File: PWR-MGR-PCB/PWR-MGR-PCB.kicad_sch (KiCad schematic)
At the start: 19 parts, among them J1 USB_C_Receptacle_USB2.0_14P, J2 Battery_1x2, U1 USBLC6-2SC6, U2 TLV75533PDBV, U3 BQ24074RGT

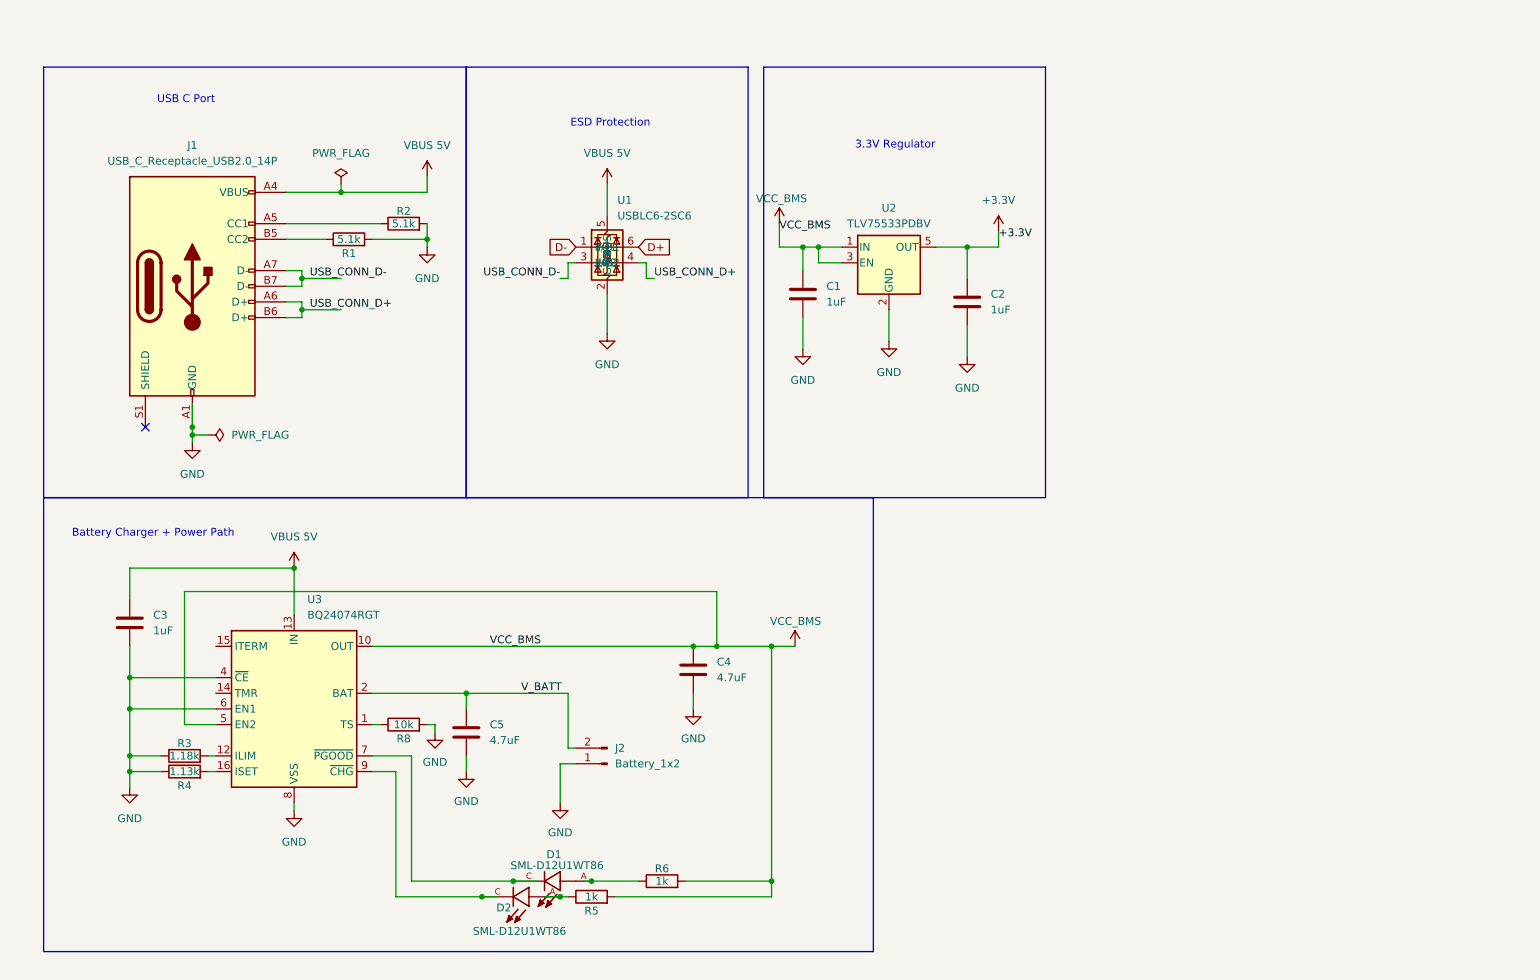
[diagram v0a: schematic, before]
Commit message: Add test ports
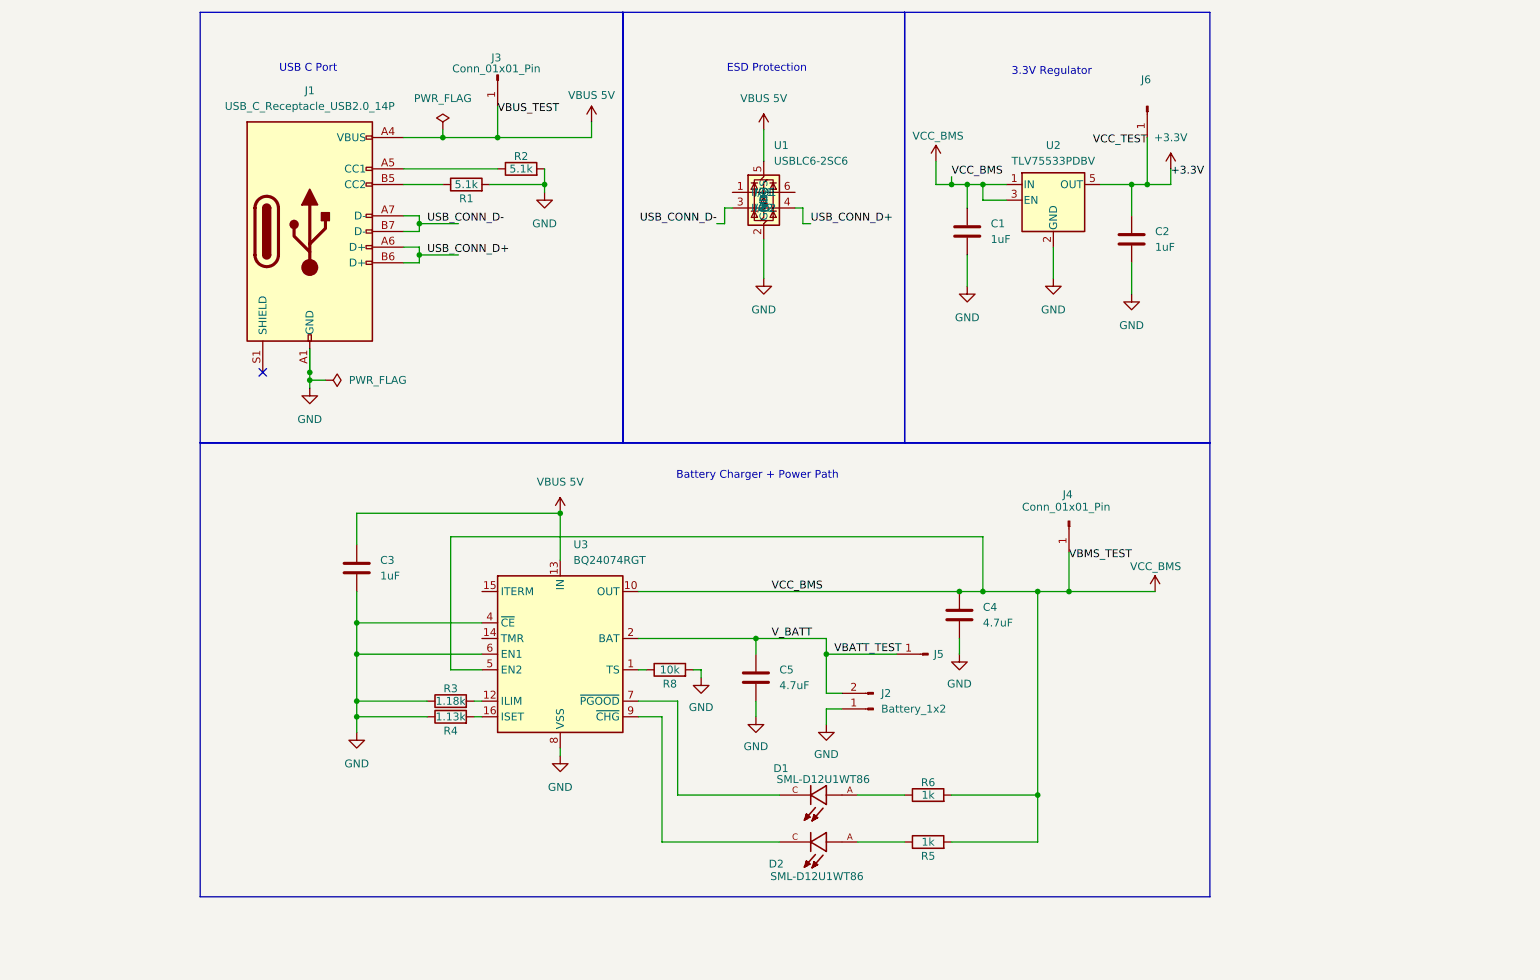
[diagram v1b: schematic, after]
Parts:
- added J3, J4, J5, J6: Conn_01x01_Pin, Connector_PinSocket_2.54mm:PinSocket_1x01_P2.54mm_Vertical, symbol Connector:Conn_01x01_Pin
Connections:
- net +3.3V: now also J6.1 (Pin_1)
- net VBUS 5V: now also J3.1 (Pin_1)
- net VCC_BMS: now also J4.1 (Pin_1)
- net D+: no longer names the net of U1.6 (I/O1)
- net D-: no longer names the net of U1.1 (I/O1)
- net V_BATT renamed VBATT_TEST
- net VBATT_TEST: now also J5.1 (Pin_1)
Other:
- moved on the sheet: C1, C2, C3, C4, C5, D1, D2, J1, J2, R1, R2, R3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

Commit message: Reroute board
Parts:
- removed J1: USB_C_Receptacle_USB2.0_14P, Connector_USB:USB_C_Receptacle_GCT_USB4105-xx-A_16P_TopMnt_Horizontal, symbol Connector:USB_C_Receptacle_USB2.0_14P
- added J1: USB_C_Receptacle_USB2.0_16P, Connector_USB:USB_C_Receptacle_GCT_USB4105-xx-A_16P_TopMnt_Horizontal, symbol Connector:USB_C_Receptacle_USB2.0_16P
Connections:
- net GND: now also J1.A1 (GND), J1.A12 (GND), J1.B1 (GND), J1.B12 (GND)
- net USB_CONN_D+: now also J1.A6 (D+), J1.B6 (D+)
- net USB_CONN_D-: now also J1.A7 (D-), J1.B7 (D-)
- net VBUS 5V: now also J1.A4 (VBUS), J1.A9 (VBUS), J1.B4 (VBUS), J1.B9 (VBUS)
- net at R2.1: now also J1.A5 (CC1)
- net at R1.1: now also J1.B5 (CC2)
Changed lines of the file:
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@@
 	)
 	(junction
+		(at 76.2 78.74)
+		(diameter 0)
+		(color 0 0 0 0)
+	)
+	(junction
 		(at 182.88 46.99)
 		(diameter 0)
@@
 	)
 	(junction
-		(at 83.82 130.81)
+		(at 93.98 58.42)
 		(diameter 0)
 		(color 0 0 0 0)
 	)
 	(junction
-		(at 209.55 46.99)
+		(at 83.82 130.81)
 		(diameter 0)
 		(color 0 0 0 0)
 	)
 	(junction
-		(at 76.2 77.47)
+		(at 209.55 46.99)
 		(diameter 0)
 		(color 0 0 0 0)
@@
 	)
 	(junction
+		(at 93.98 53.34)
+		(diameter 0)
+		(color 0 0 0 0)
+	)
+	(junction
 		(at 114.3 46.99)
 		(diameter 0)
@@
 	)
 	(junction
-		(at 76.2 78.74)
+		(at 106.68 35.56)
 		(diameter 0)
 		(color 0 0 0 0)
@@
 	)
 	(junction
-		(at 93.98 53.34)
-		(diameter 0)
-		(color 0 0 0 0)
-	)
-	(junction
 		(at 83.82 118.11)
 		(diameter 0)
@@
 		(color 0 0 0 0)
 	)
-	(junction
-		(at 93.98 58.42)
-		(diameter 0)
-		(color 0 0 0 0)
-	)
 	(no_connect
 		(at 68.58 77.47)
@@
 	(wire
 		(pts
-			(xy 106.68 34.29) (xy 106.68 39.37)
+			(xy 76.2 78.74) (xy 76.2 80.01)
+		)
+		(stroke
+			(width 0)
+			(type default)
+		)
+	)
+	(wire
+		(pts
+			(xy 106.68 34.29) (xy 106.68 35.56)
 		)
 		(stroke
@@
 	(wire
 		(pts
+			(xy 76.2 78.74) (xy 78.74 78.74)
+		)
+		(stroke
+			(width 0)
+			(type default)
+		)
+	)
+	(wire
+		(pts
 			(xy 83.82 130.81) (xy 83.82 133.35)
 		)
@@
 	(wire
 		(pts
-			(xy 76.2 78.74) (xy 78.74 78.74)
+			(xy 76.2 77.47) (xy 76.2 78.74)
 		)
 		(stroke
@@
 	(wire
 		(pts
-			(xy 180.34 45.72) (xy 180.34 46.99)
+			(xy 93.98 54.61) (xy 93.98 53.34)
 		)
 		(stroke
@@
 	(wire
 		(pts
-			(xy 194.31 113.03) (xy 194.31 146.05)
+			(xy 180.34 45.72) (xy 180.34 46.99)
 		)
 		(stroke
@@
 	(wire
 		(pts
-			(xy 83.82 100.33) (xy 116.84 100.33)
+			(xy 93.98 58.42) (xy 93.98 57.15)
 		)
 		(stroke
@@
 	(wire
 		(pts
-			(xy 76.2 73.66) (xy 76.2 77.47)
+			(xy 194.31 113.03) (xy 194.31 146.05)
 		)
 		(stroke
@@
 	(wire
 		(pts
-			(xy 148.59 120.65) (xy 148.59 123.19)
+			(xy 83.82 100.33) (xy 116.84 100.33)
 		)
 		(stroke
@@
 	(wire
 		(pts
-			(xy 76.2 78.74) (xy 76.2 80.01)
+			(xy 148.59 120.65) (xy 148.59 123.19)
 		)
 		(stroke
@@
 	(wire
 		(pts
-			(xy 91.44 46.99) (xy 97.79 46.99)
+			(xy 204.47 46.99) (xy 209.55 46.99)
 		)
 		(stroke
@@
 	(wire
 		(pts
-			(xy 204.47 46.99) (xy 209.55 46.99)
+			(xy 93.98 52.07) (xy 93.98 53.34)
 		)
 		(stroke
@@
 	(wire
 		(pts
-			(xy 143.51 50.8) (xy 144.78 50.8)
+			(xy 107.95 35.56) (xy 106.68 35.56)
 		)
 		(stroke
@@
 	(wire
 		(pts
-			(xy 139.7 127) (xy 139.7 125.73)
+			(xy 97.79 39.37) (xy 97.79 38.1)
 		)
 		(stroke
@@
 	(wire
 		(pts
-			(xy 76.2 77.47) (xy 76.2 78.74)
+			(xy 143.51 50.8) (xy 144.78 50.8)
 		)
 		(stroke
@@
 	(wire
 		(pts
-			(xy 160.02 129.54) (xy 160.02 123.19)
+			(xy 139.7 127) (xy 139.7 125.73)
 		)
 		(stroke
@@
 	(wire
 		(pts
-			(xy 114.3 46.99) (xy 114.3 48.26)
+			(xy 160.02 129.54) (xy 160.02 123.19)
 		)
 		(stroke
@@
 	(wire
 		(pts
-			(xy 93.98 58.42) (xy 93.98 59.69)
+			(xy 114.3 46.99) (xy 114.3 48.26)
 		)
 		(stroke
@@
 	(wire
 		(pts
-			(xy 97.79 38.1) (xy 97.79 39.37)
+			(xy 93.98 59.69) (xy 93.98 58.42)
 		)
 		(stroke
@@
 	(wire
 		(pts
-			(xy 93.98 52.07) (xy 93.98 53.34)
-		)
-		(stroke
-			(width 0)
-			(type default)
-		)
-	)
-	(wire
-		(pts
 			(xy 180.34 146.05) (xy 194.31 146.05)
 		)
@@
 	(wire
 		(pts
-			(xy 93.98 53.34) (xy 93.98 54.61)
-		)
-		(stroke
-			(width 0)
-			(type default)
-		)
-	)
-	(wire
-		(pts
 			(xy 156.21 50.8) (xy 154.94 50.8)
 		)
@@
 	(wire
 		(pts
+			(xy 91.44 46.99) (xy 97.79 46.99)
+		)
+		(stroke
+			(width 0)
+			(type default)
+		)
+	)
+	(wire
+		(pts
 			(xy 156.21 53.34) (xy 156.21 50.8)
 		)
@@
 	(wire
 		(pts
-			(xy 93.98 57.15) (xy 93.98 58.42)
-		)
-		(stroke
-			(width 0)
-			(type default)
-		)
-	)
-	(wire
-		(pts
 			(xy 83.82 133.35) (xy 83.82 135.89)
 		)
@@
 		)
 	)
+	(wire
+		(pts
+			(xy 106.68 35.56) (xy 106.68 39.37)
+		)
+		(stroke
+			(width 0)
+			(type default)
+		)
+	)
 	(label "USB_CONN_D+"
 		(at 95.25 58.42 0)
@@
 	)
 	(label "VBUS_TEST"
-		(at 106.68 35.56 0)
+		(at 107.95 35.56 0)
 		(effects
 			(font
@@
 	)
 	(symbol
-		(lib_id "Connector:USB_C_Receptacle_USB2.0_14P")
-		(at 76.2 54.61 0)
-		(unit 1)
-		(exclude_from_sim no)
-		(in_bom yes)
-		(on_board yes)
-		(dnp no)
-		(fields_autoplaced yes)
-		(property "Reference" "J1"
-			(at 76.2 31.75 0)
-			(effects
-				(font
-					(size 1.27 1.27)
-				)
-			)
-		)
-		(property "Value" "USB_C_Receptacle_USB2.0_14P"
-			(at 76.2 34.29 0)
-			(effects
-				(font
-					(size 1.27 1.27)
-				)
-			)
-		)
-		(property "Footprint" "Connector_USB:USB_C_Receptacle_GCT_USB4105-xx-A_16P_TopMnt_Horizontal"
-			(at 80.01 54.61 0)
-			(effects
-				(font
-					(size 1.27 1.27)
-				)
-				(hide yes)
-			)
-		)
-		(property "Datasheet" "https://www.usb.org/sites/default/files/documents/usb_type-c.zip"
-			(at 80.01 54.61 0)
-			(effects
-				(font
-					(size 1.27 1.27)
-				)
-				(hide yes)
-			)
-		)
-		(property "Description" "USB 2.0-only 14P Type-C Receptacle connector"
-			(at 76.2 54.61 0)
-			(effects
-				(font
-					(size 1.27 1.27)
-				)
-				(hide yes)
-			)
-		)
-		(pin "A12"
-		)
-		(pin "B9"
-		)
-		(pin "A7"
-		)
-		(pin "A9"
-		)
-		(pin "A6"
-		)
-		(pin "A5"
-		)
-		(pin "B4"
-		)
-		(pin "B6"
-		)
-		(pin "B1"
-		)
-		(pin "S1"
-		)
-		(pin "A4"
-		)
-		(pin "B5"
-		)
-		(pin "A1"
-		)
-		(pin "B12"
-		)
-		(pin "B7"
-		)
-		(instances
-			(project "PWR-MGR-PCB"
-				(path "/16b2e4e2-6399-42b6-a8e6-a11780888710"
-					(reference "J1")
-					(unit 1)
-				)
-			)
-		)
-	)
-	(symbol
 		(lib_id "Connector:Conn_01x02_Pin")
 		(at 167.64 132.08 180)
@@
 					(unit 1)
 				)
+			)
+		)
+	)
+	(symbol
+		(lib_id "Connector:USB_C_Receptacle_USB2.0_16P")
+		(at 76.2 54.61 0)
+		(unit 1)
+		(exclude_from_sim no)
+		(in_bom yes)
+		(on_board yes)
+		(dnp no)
+		(fields_autoplaced yes)
+		(property "Reference" "J1"
+			(at 76.2 31.75 0)
+			(effects
+				(font
+					(size 1.27 1.27)
+				)
+			)
+		)
+		(property "Value" "USB_C_Receptacle_USB2.0_16P"
+			(at 76.2 34.29 0)
+			(effects
+				(font
+					(size 1.27 1.27)
+				)
+			)
+		)
+		(property "Footprint" "Connector_USB:USB_C_Receptacle_GCT_USB4105-xx-A_16P_TopMnt_Horizontal"
+			(at 80.01 54.61 0)
+			(effects
+				(font
+					(size 1.27 1.27)
+				)
+				(hide yes)
+			)
+		)
+		(property "Datasheet" "https://www.usb.org/sites/default/files/documents/usb_type-c.zip"
+			(at 80.01 54.61 0)
+			(effects
+				(font
+					(size 1.27 1.27)
+				)
+				(hide yes)
+			)
+		)
+		(property "Description" "USB 2.0-only 16P Type-C Receptacle connector"
+			(at 76.2 54.61 0)
+			(effects
+				(font
+					(size 1.27 1.27)
+				)
+				(hide yes)
+			)
+		)
+		(pin "B6"
+		)
+		(pin "A12"
+		)
+		(pin "A9"
+		)
+		(pin "A4"
+		)
+		(pin "B9"
+		)
+		(pin "B5"
+		)
+		(pin "B12"
+		)
+		(pin "B8"
+		)
+		(pin "B4"
+		)
+		(pin "B7"
+		)
+		(pin "S1"
+		)
+		(pin "A7"
+		)
+		(pin "B1"
+		)
+		(pin "A1"
+		)
+		(pin "A5"
+		)
+		(pin "A6"
+		)
+		(pin "A8"
+		)
+		(instances
+			(project ""
+				(path "/16b2e4e2-6399-42b6-a8e6-a11780888710"
+					(reference "J1")
+					(unit 1)
+				)

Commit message: Sync latest fixes
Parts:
- removed J1: USB_C_Receptacle_USB2.0_16P, Connector_USB:USB_C_Receptacle_GCT_USB4105-xx-A_16P_TopMnt_Horizontal, symbol Connector:USB_C_Receptacle_USB2.0_16P
- removed J3, J4, J5, J6: Conn_01x01_Pin, Connector_PinSocket_2.54mm:PinSocket_1x01_P2.54mm_Vertical, symbol Connector:Conn_01x01_Pin
- added D3: 1N5400, Diode_THT:D_DO-201AD_P15.24mm_Horizontal, symbol Diode:1N5400
- added J1: USB_C_Receptacle_USB2.0_14P, Connector_USB:USB_C_Receptacle_GCT_USB4105-xx-A_16P_TopMnt_Horizontal, symbol Connector:USB_C_Receptacle_USB2.0_14P
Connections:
- net GND: now also J1.A1 (GND), J1.A12 (GND), J1.B1 (GND), J1.B12 (GND), J1.S1 (SHIELD)
- net USB_CONN_D+: now also U1.1 (I/O1), J1.A6 (D+), J1.B6 (D+); no longer U1.4 (I/O2)
- net USB_CONN_D-: now also J1.A7 (D-), J1.B7 (D-)
- net VBUS 5V: now also D3.1 (K)
- net at R2.1: now also J1.A5 (CC1)
- net at R1.1: now also J1.B5 (CC2)
- net D+: now reaches U1.6 (I/O1)
- net VBATT_TEST renamed V_BATT
- new net: D3.2 (A), J1.A4 (VBUS), J1.A9 (VBUS), J1.B4 (VBUS), J1.B9 (VBUS)
- new net D-: U1.4 (I/O2)
- no-connect marks 1 -> 2
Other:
- note added: "Voltage divider on enable pin can cutoff battery to prevent excessive drain (not included)"
- moved on the sheet: C1, C2, C3, C4, C5, D1, D2, J2, R1, R2, R3, R4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

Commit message: Update diode component
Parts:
- removed D3: 1N5400, Diode_THT:D_DO-201AD_P15.24mm_Horizontal, symbol Diode:1N5400
- added D4: SS34, Diode_SMD:D_SMA, symbol Diode:SS34
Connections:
- net VBUS 5V: now also D4.1 (K)
- net at J1.A4 (VBUS), J1.A9 (VBUS), J1.B4 (VBUS)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: now also D4.2 (A)
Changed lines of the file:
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@@
-	)
-	(symbol
-		(lib_id "Diode:1N5400")
-		(at 82.55 48.26 180)
-		(unit 1)
-		(exclude_from_sim no)
-		(in_bom yes)
-		(on_board yes)
-		(dnp no)
-		(fields_autoplaced yes)
-		(property "Reference" "D3"
-			(at 82.55 41.91 0)
-			(effects
-				(font
-					(size 1.27 1.27)
-				)
-			)
-		)
-		(property "Value" "1N5400"
-			(at 82.55 45.212 0)
-			(effects
-				(font
-					(size 1.27 1.27)
-				)
-			)
-		)
-		(property "Footprint" "Diode_THT:D_DO-201AD_P15.24mm_Horizontal"
-			(at 82.55 43.815 0)
-			(effects
-				(font
-					(size 1.27 1.27)
-				)
-				(hide yes)
-			)
-		)
-		(property "Datasheet" "http://www.vishay.com/docs/88516/1n5400.pdf"
-			(at 82.55 48.26 0)
-			(effects
-				(font
-					(size 1.27 1.27)
-				)
-				(hide yes)
-			)
-		)
-		(property "Description" "50V 3A General Purpose Rectifier Diode, DO-201AD"
-			(at 82.55 48.26 0)
-			(effects
-				(font
-					(size 1.27 1.27)
-				)
-				(hide yes)
-			)
-		)
-		(property "Sim.Device" "D"
-			(at 82.55 48.26 0)
-			(effects
-				(font
-					(size 1.27 1.27)
-				)
-				(hide yes)
-			)
-		)
-		(property "Sim.Pins" "1=K 2=A"
-			(at 82.55 48.26 0)
-			(effects
-				(font
-					(size 1.27 1.27)
-				)
-				(hide yes)
-			)
-		)
-		(pin "2"
-		)
-		(pin "1"
-		)
-		(instances
-			(project "PWR-MGR-PCB"
-				(path "/16b2e4e2-6399-42b6-a8e6-a11780888710"
-					(reference "D3")
-					(unit 1)
-				)
-			)
-		)
 	)
 	(symbol
@@
 					(unit 1)
 				)
+			)
+		)
+	)
+	(symbol
+		(lib_id "Diode:SS34")
+		(at 82.55 48.26 180)
+		(unit 1)
+		(exclude_from_sim no)
+		(in_bom yes)
+		(on_board yes)
+		(dnp no)
+		(fields_autoplaced yes)
+		(property "Reference" "D4"
+			(at 82.8675 41.91 0)
+			(effects
+				(font
+					(size 1.27 1.27)
+				)
+			)
+		)
+		(property "Value" "SS34"
+			(at 82.8675 44.45 0)
+			(effects
+				(font
+					(size 1.27 1.27)
+				)
+			)
+		)
+		(property "Footprint" "Diode_SMD:D_SMA"
+			(at 82.55 43.815 0)
+			(effects
+				(font
+					(size 1.27 1.27)
+				)
+				(hide yes)
+			)
+		)
+		(property "Datasheet" "https://www.vishay.com/docs/88751/ss32.pdf"
+			(at 82.55 48.26 0)
+			(effects
+				(font
+					(size 1.27 1.27)
+				)
+				(hide yes)
+			)
+		)
+		(property "Description" "40V 3A Schottky Diode, SMA"
+			(at 82.55 48.26 0)
+			(effects
+				(font
+					(size 1.27 1.27)
+				)
+				(hide yes)
+			)
+		)
+		(pin "1"
+		)
+		(pin "2"
+		)
+		(instances
+			(project ""
+				(path "/16b2e4e2-6399-42b6-a8e6-a11780888710"
+					(reference "D4")
+					(unit 1)
+				)

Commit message: Replace LDO with buck boost converter
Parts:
- added C6: 1uF, Capacitor_SMD:C_0805_2012Metric, symbol Device:C
- added L1: DFE18SAN1R0ME0L, DFE18SAN1R0ME0L:INDC1608X80N, symbol DFE18SAN1R0ME0L:DFE18SAN1R0ME0L
- added U4: TPS631011YBGR, DSBGA8_YBG_TEX, symbol TPS631011:TPS631011YBGR
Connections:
- net GND: now also C6.2, U4.C2 (GND)
- net VCC_BMS: now also C6.1, U4.A1 (VIN)

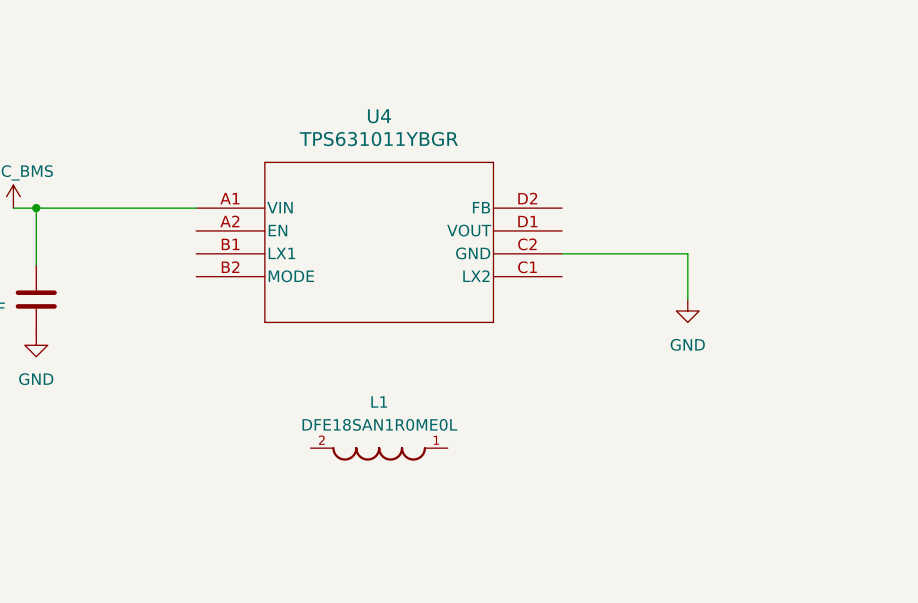
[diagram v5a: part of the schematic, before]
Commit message: Add inductor
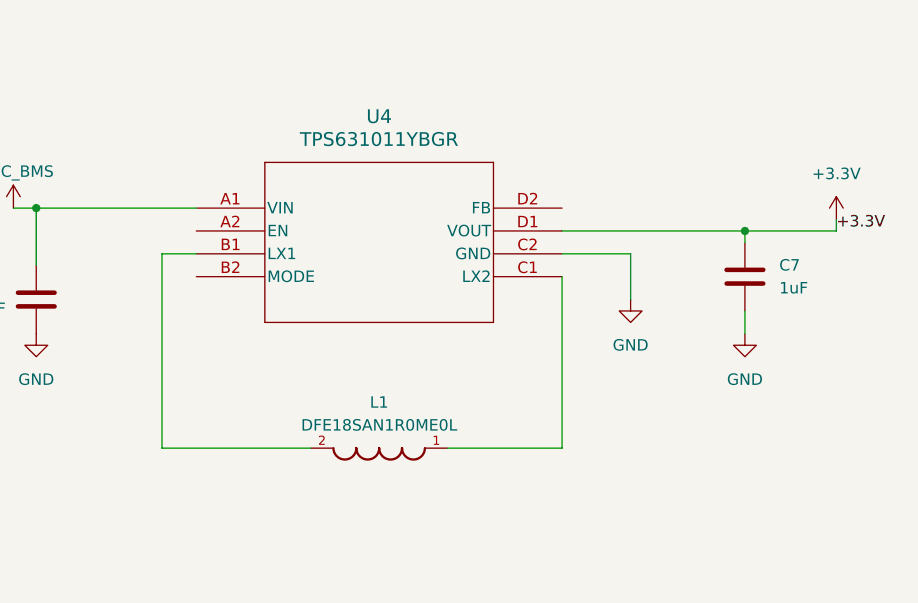
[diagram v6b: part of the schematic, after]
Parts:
- added C7: 1uF, Capacitor_SMD:C_0805_2012Metric, symbol Device:C
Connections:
- net +3.3V: now also U4.D1 (VOUT), C7.1
- net GND: now also C7.2
- net at L1.1: now also U4.C1 (LX2)
- net at L1.2: now also U4.B1 (LX1)
